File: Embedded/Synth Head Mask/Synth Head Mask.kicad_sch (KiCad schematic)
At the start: 0 parts

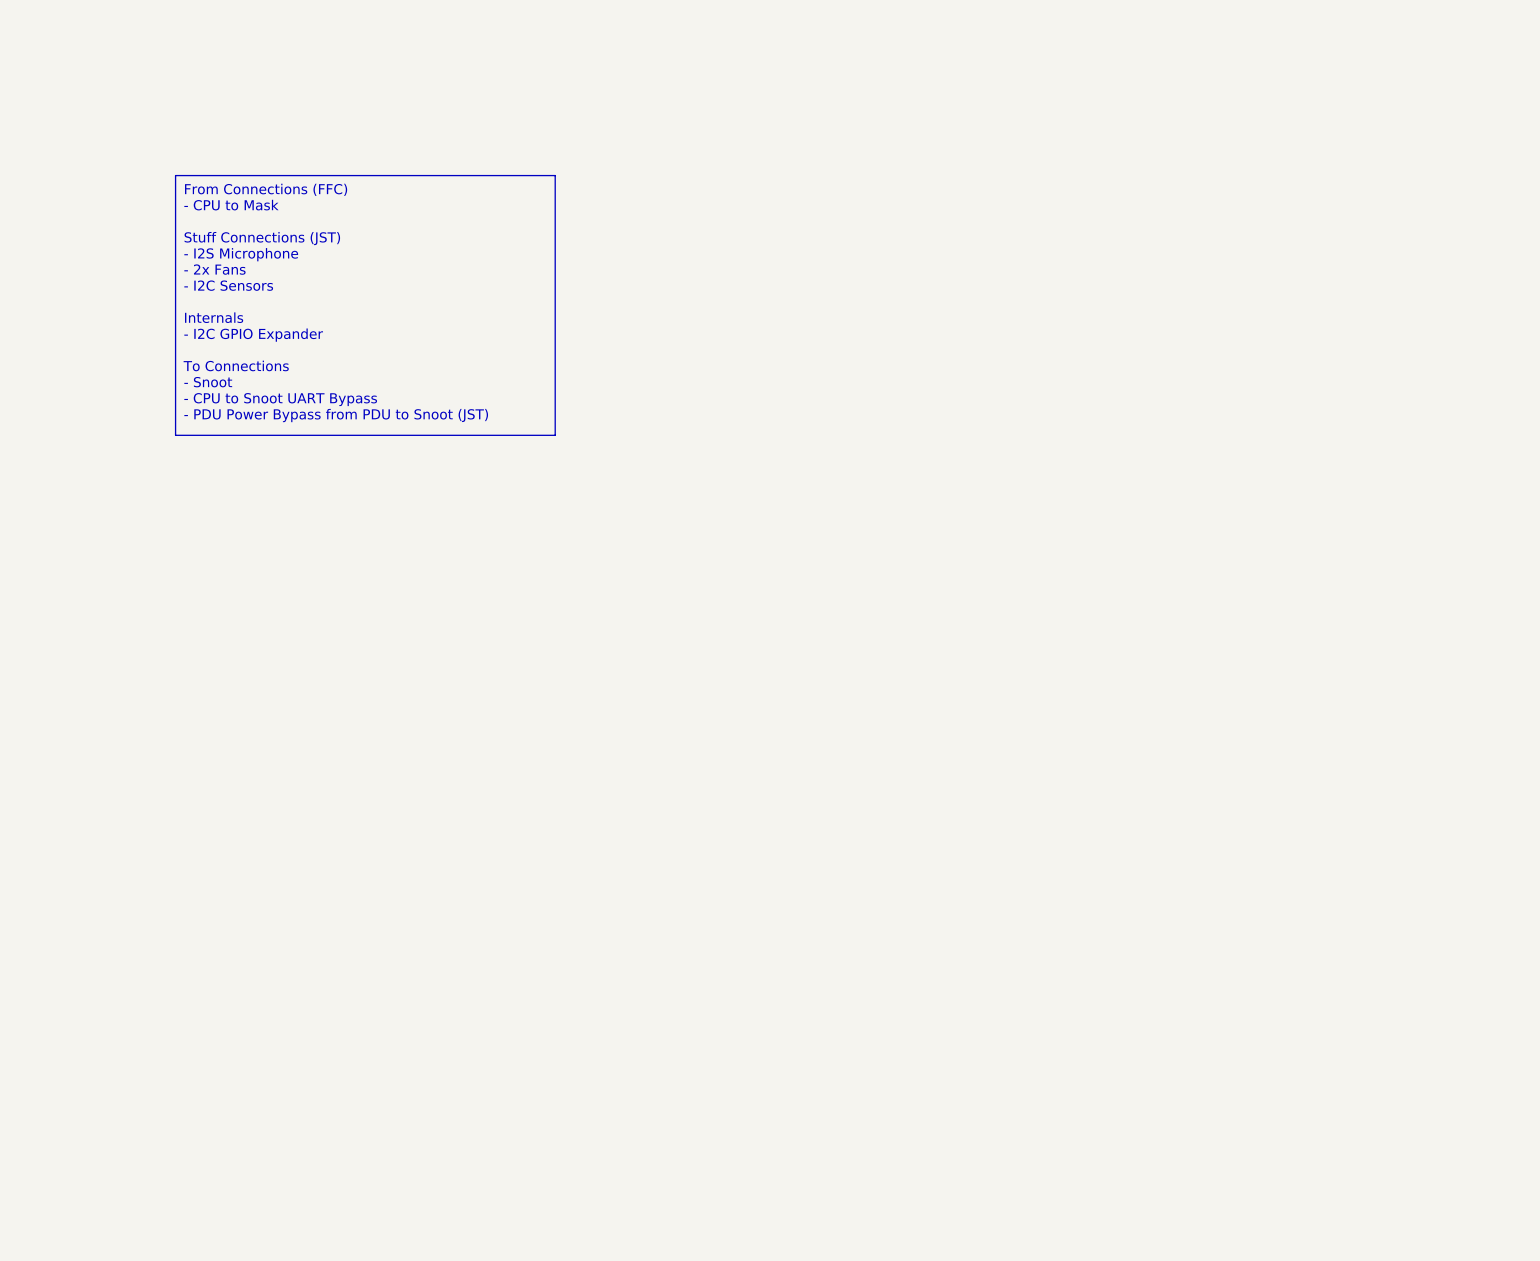
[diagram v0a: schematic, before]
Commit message: Majority of the pins for the Mask Board & Snoot Added
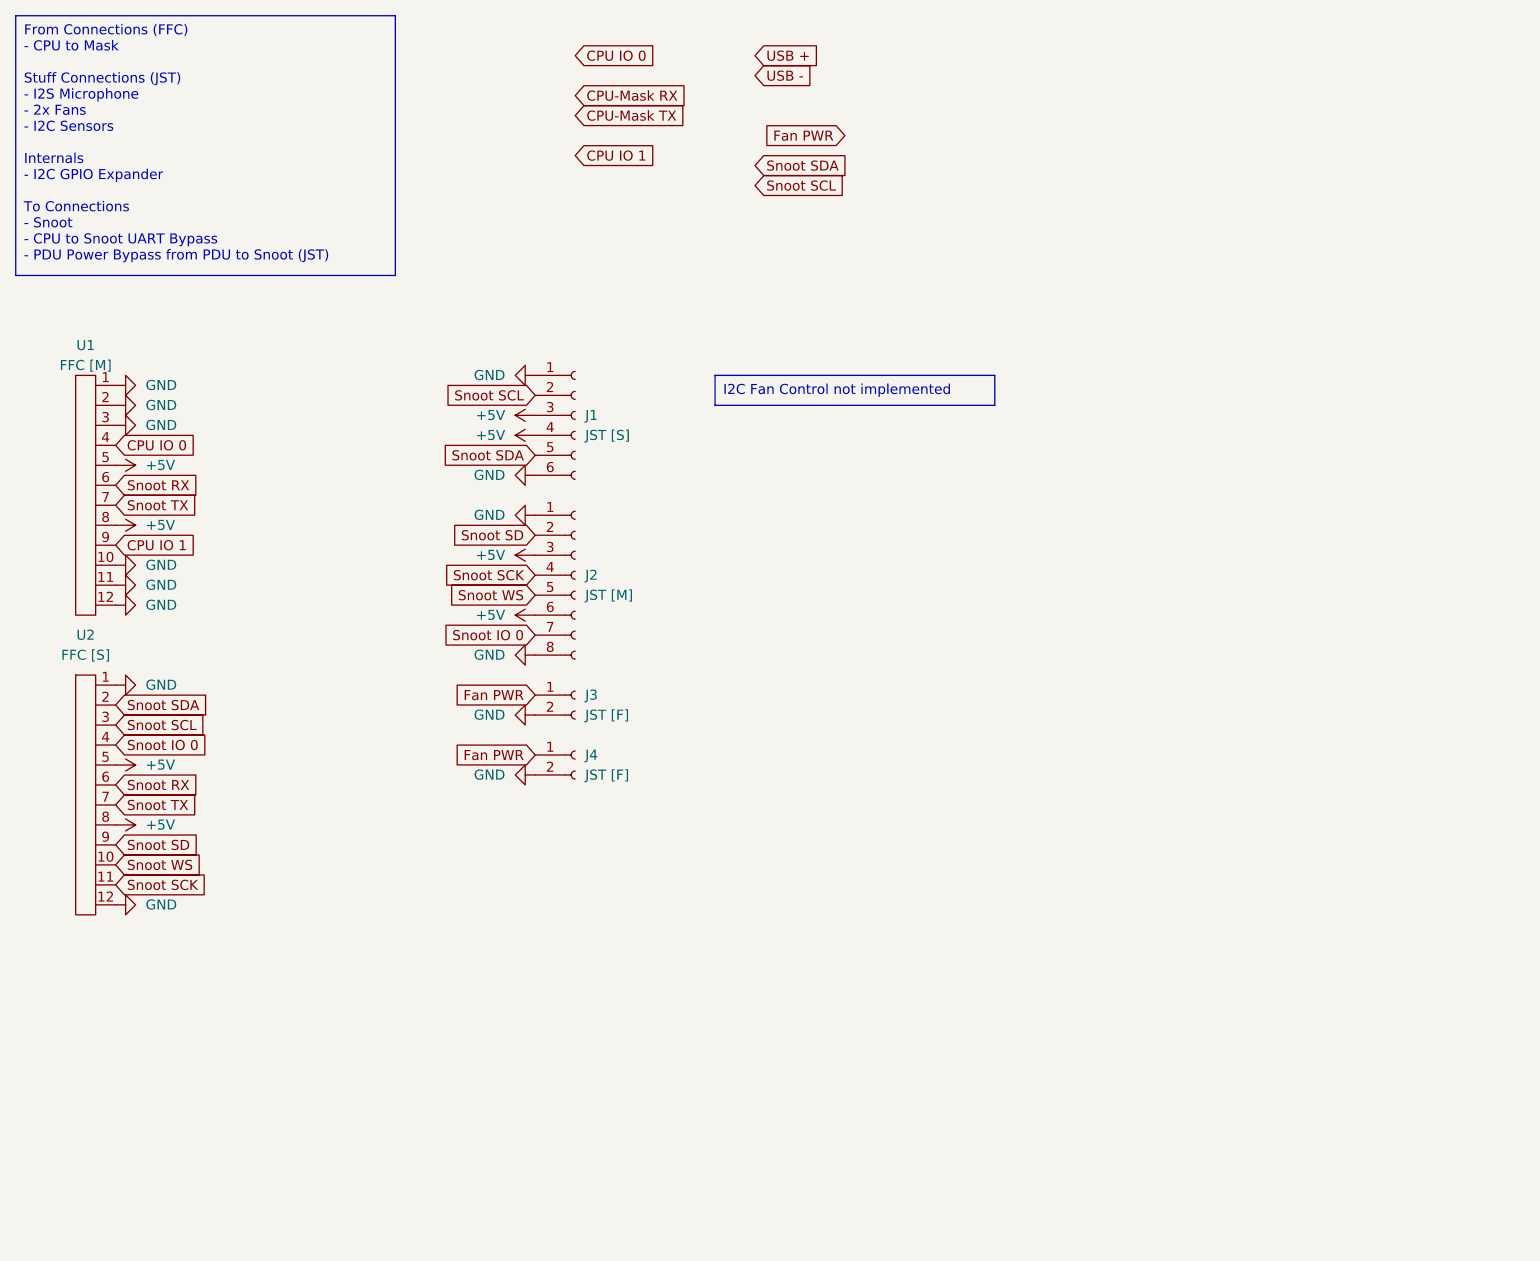
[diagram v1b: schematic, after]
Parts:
- added J1: JST [S], symbol Connector:Conn_01x06_Socket
- added J2: JST [M], symbol Connector:Conn_01x08_Socket
- added J3, J4: JST [F], symbol Connector:Conn_01x02_Socket
- added U1: FFC [M], FFC_Connector:FFC Aliexpress 0.5mm 12P, symbol FCC_Connector:FFC_12P
- added U2: FFC [S], FFC_Connector:FFC Aliexpress 0.5mm 12P, symbol FCC_Connector:FFC_12P
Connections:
- new net +5V: J1.3 (Pin_3), J1.4 (Pin_4), J2.3 (Pin_3), J2.6 (Pin_6), U1.5, U1.8, U2.5, U2.8
- new net CPU IO 0: U1.4
- new net CPU IO 1: U1.9
- new net Fan PWR: J3.1 (Pin_1), J4.1 (Pin_1)
- new net GND: J1.1 (Pin_1), J1.6 (Pin_6), J2.1 (Pin_1), J2.8 (Pin_8), J3.2 (Pin_2), J4.2 (Pin_2), U1.1, U1.10, U1.11, U1.12, U1.2, U1.3, U2.1, U2.12
- new net Snoot IO 0: J2.7 (Pin_7), U2.4
- new net Snoot RX: U1.6, U2.6
- new net Snoot SCK: J2.4 (Pin_4), U2.11
- new net Snoot SCL: J1.2 (Pin_2), U2.3
- new net Snoot SD: J2.2 (Pin_2), U2.9
- new net Snoot SDA: J1.5 (Pin_5), U2.2
- new net Snoot TX: U1.7, U2.7
- new net Snoot WS: J2.5 (Pin_5), U2.10

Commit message: Nearly completed Mask Board
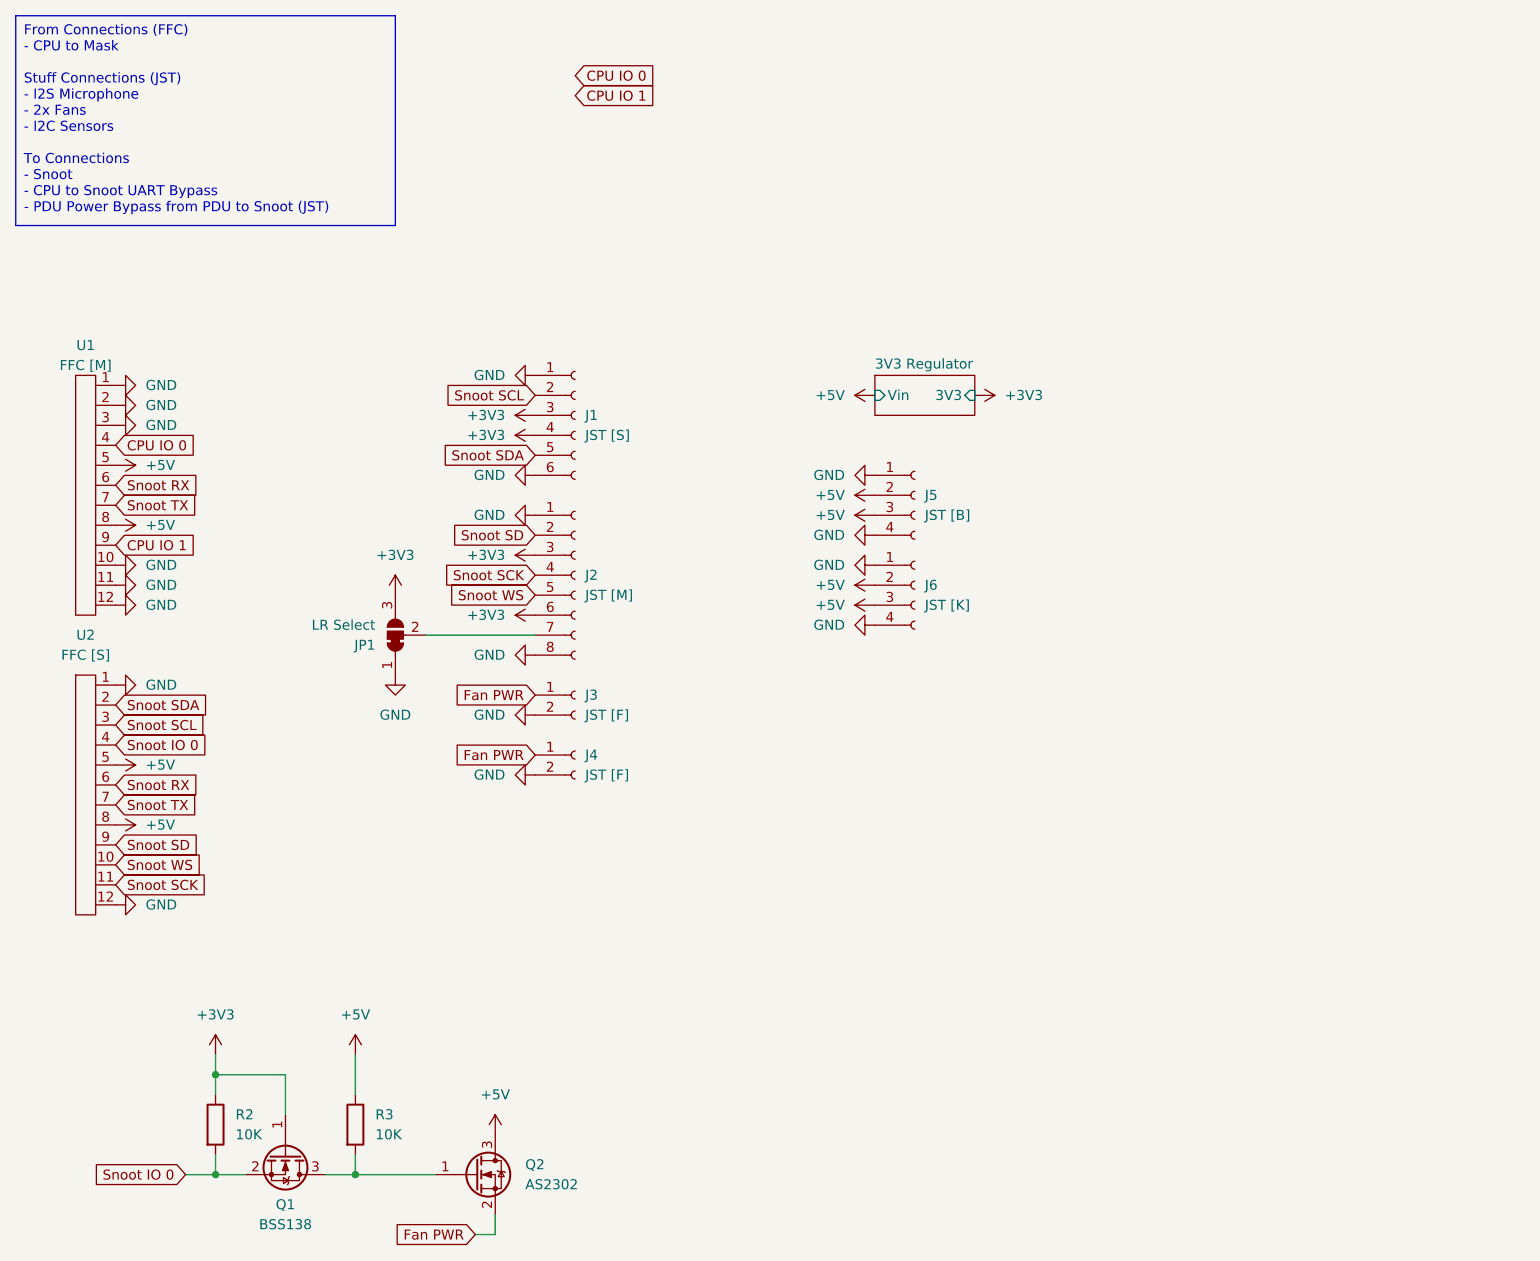
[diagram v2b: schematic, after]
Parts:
- added J5: JST [B], symbol Connector:Conn_01x04_Socket
- added J6: JST [K], symbol Connector:Conn_01x04_Socket
- added JP1: LR Select, symbol Jumper:SolderJumper_3_Bridged12
- added Q1: BSS138, Package_TO_SOT_SMD:SOT-23, symbol Transistor_FET:BSS138
- added Q2: AS2302, Package_TO_SOT_SMD:SOT-23, symbol Transistor_FET:BSS138
- added R2, R3: 10K, symbol Device:R
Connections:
- net +5V: now also J5.2 (Pin_2), J5.3 (Pin_3), J6.2 (Pin_2), J6.3 (Pin_3), Q2.3 (D), R3.1; no longer J1.3 (Pin_3), J1.4 (Pin_4), J2.3 (Pin_3), J2.6 (Pin_6)
- net Fan PWR: now also Q2.2 (S)
- net GND: now also J5.1 (Pin_1), J5.4 (Pin_4), J6.1 (Pin_1), J6.4 (Pin_4), JP1.1 (A)
- net Snoot IO 0: now also Q1.2 (S), R2.2; no longer J2.7 (Pin_7)
- new net: J2.7 (Pin_7), JP1.2 (C)
- new net: Q1.3 (D), Q2.1 (G), R3.2
- new net +3V3: J1.3 (Pin_3), J1.4 (Pin_4), J2.3 (Pin_3), J2.6 (Pin_6), JP1.3 (B), Q1.1 (G), R2.1
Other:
- added sheet 3V3 Regulator (3V3 Reg.kicad_sch)

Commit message: Prepared All Main Boards for PCB Creation
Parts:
- removed J1: JST [S], symbol Connector:Conn_01x06_Socket
- added J1: JST [S], Connector_Molex:Molex_PicoBlade_53047-0810_1x08_P1.25mm_Vertical, symbol Connector:Conn_01x08_Socket
- added J7, J8: Misc Expansion, Connector_PinHeader_2.54mm:PinHeader_1x03_P2.54mm_Vertical, symbol Connector:Conn_01x03_Socket
- added JP2, JP3: Expansion PWR, Jumper:SolderJumper-3_P1.3mm_Bridged2Bar12_Pad1.0x1.5mm, symbol Jumper:SolderJumper_3_Bridged12
- J2: footprint (none) -> Connector_Molex:Molex_PicoBlade_53047-0810_1x08_P1.25mm_Vertical
- J3, J4: footprint (none) -> Connector_Molex:Molex_PicoBlade_53047-0210_1x02_P1.25mm_Vertical
- J5, J6: footprint (none) -> Connector_Molex:Molex_PicoBlade_53047-0410_1x04_P1.25mm_Vertical
- JP1: footprint (none) -> Jumper:SolderJumper-3_P1.3mm_Bridged12_RoundedPad1.0x1.5mm
- R2, R3: footprint (none) -> Resistor_SMD:R_0603_1608Metric_Pad0.98x0.95mm_HandSolder
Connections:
- net +3V3: now also J1.3 (Pin_3), J1.6 (Pin_6), JP2.1 (A), JP3.1 (A)
- net +5V: now also JP2.3 (B), JP3.3 (B)
- net CPU IO 0: now also J7.2 (Pin_2)
- net CPU IO 1: now also J8.2 (Pin_2)
- net GND: now also J1.1 (Pin_1), J1.2 (Pin_2), J1.7 (Pin_7), J1.8 (Pin_8), J7.3 (Pin_3), J8.3 (Pin_3)
- net Snoot SCL: now also J1.4 (Pin_4)
- net Snoot SDA: now also J1.5 (Pin_5)
- new net: J8.1 (Pin_1), JP3.2 (C)
- new net: J7.1 (Pin_1), JP2.2 (C)
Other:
- moved on the sheet: J2, J3, J4, J6, JP1
